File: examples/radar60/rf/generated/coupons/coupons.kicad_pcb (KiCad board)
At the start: 6 copper layers, 60 x 25 mm, 97 parts, among them J60A SMA-J-P-H-ST-EM1, J60B SMA-J-P-H-ST-EM1, J61A SMA-J-P-H-ST-EM1, J61B SMA-J-P-H-ST-EM1, J6RA SMA-J-P-H-ST-EM1, J6RB SMA-J-P-H-ST-EM1

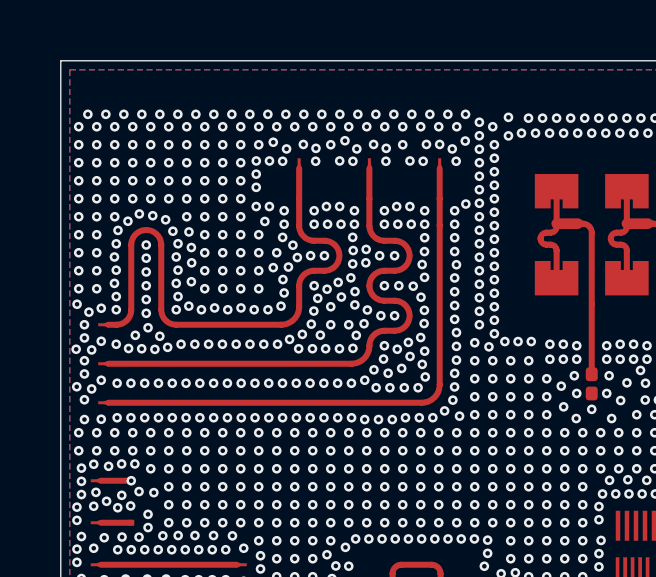
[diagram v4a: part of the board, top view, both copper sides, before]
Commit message: radar60 rf: stage 3b generator options, D14 PA feed, D15 pour variants, E1 models
Generator (examples/radar60/rf/rfmacro):
- D14: the macro owns the VOUT_PA (1V0_PA) feed: A2/B2 bar, a neck east of row A
  inside the package outline, four 0.20/0.40 vias in the pocket (board rules
  unchanged; PWR clearance 0.15 mm), an In3 tie stand-in, board_frame.pa_feed
  hand-off (skip_pads A2/B2). New check G8: clearances, pocket, L2 anti-pads,
  current per via, IR drop [D].
- D15: pour presets A (0.60 mm grid), B (1.00 mm grid, interior hard maximum
  0.75 mm), C (GCPW strips, rings, isolation, load cells; L2-L3 lattice). G3 has
  edge and interior thresholds and an L2-L3 check; stitch metrics per record.
- Dummies S1 / S1.5 and DNP loads ("short" refused); G2 declares the edge
  columns S1 leaves without a neighbour.
- L2-L3 cavity options K0 / K2 (posts, column-congruent) / K1; check G9.
- C1 / D5: div_l_scale and a series-fed column in the bank.
- TX: T2 (R 0.75 north-west finger), T4 (TX1 within a skew budget), T3 order
  planarity; the fit keeps lines out of load mask islands.
- Via placement closes fence gaps a shared row leaves (chain shift, row
  re-plan); known limit: T2's lane-finger junction keeps a 0.65 mm gap (G4).
- `rfmacro variants`: the 14 stage-3b boards; rfm1-m/n/p and coupons rebuilt.

EM (openems): triplet / centre-only cells from the generator, plane-pair
ring-down (board_pp, pp_sim), PA corner (board_pa, pa_sim), mesh templates
(ant_sim --mesh-ref), the E1 campaign builder (stage3b_em.py), results/stage3b.

Co-Authored-By: Claude Opus 5.5 <noreply@anthropic.com>
Claude-Session: https://claude.ai/code/session_014FiHUDEn5jCP4V8pPjQkPy
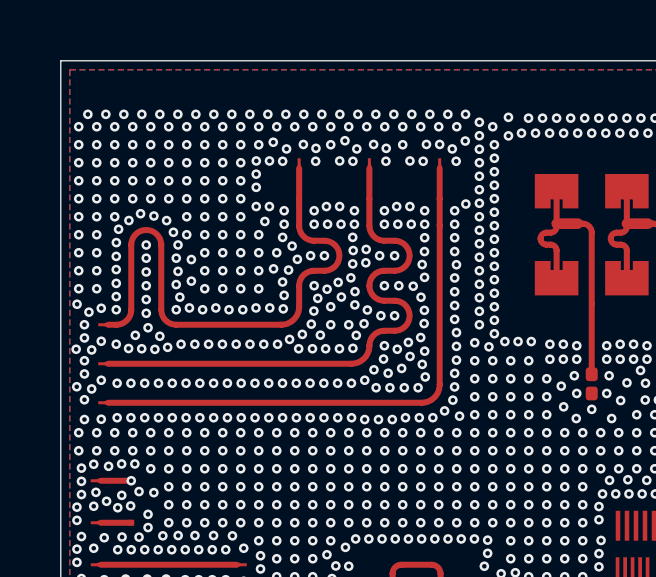
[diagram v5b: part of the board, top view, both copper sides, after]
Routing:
- net GND: vias 1843 -> 1842
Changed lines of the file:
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@@
 	(via (at 113.131 80.9) (size 0.32) (drill 0.15) (layers "F.Cu" "B.Cu") (net "GND"))
 	(via (at 101.85 82.86032) (size 0.32) (drill 0.15) (layers "F.Cu" "B.Cu") (net "GND"))
-	(via (at 101.79 82.42065) (size 0.32) (drill 0.15) (layers "F.Cu" "B.Cu") (net "GND"))
-	(via (at 101.85 81.98097) (size 0.32) (drill 0.15) (layers "F.Cu" "B.Cu") (net "GND"))
-	(via (at 101.79 81.5413) (size 0.32) (drill 0.15) (layers "F.Cu" "B.Cu") (net "GND"))
-	(via (at 101.85079 81.10184) (size 0.32) (drill 0.15) (layers "F.Cu" "B.Cu") (net "GND"))
-	(via (at 101.90842 80.65474) (size 0.32) (drill 0.15) (layers "F.Cu" "B.Cu") (net "GND"))
-	(via (at 102.23992 80.34925) (size 0.32) (drill 0.15) (layers "F.Cu" "B.Cu") (net "GND"))
-	(via (at 102.62 80.10685) (size 0.32) (drill 0.15) (layers "F.Cu" "B.Cu") (net "GND"))
-	(via (at 103.06698 80.16542) (size 0.32) (drill 0.15) (layers "F.Cu" "B.Cu") (net "GND"))
-	(via (at 103.49668 80.30171) (size 0.32) (drill 0.15) (layers "F.Cu" "B.Cu") (net "GND"))
-	(via (at 103.73828 80.6823) (size 0.32) (drill 0.15) (layers "F.Cu" "B.Cu") (net "GND"))
-	(via (at 103.90913 81.09877) (size 0.32) (drill 0.15) (layers "F.Cu" "B.Cu") (net "GND"))
-	(via (at 103.85 81.5413) (size 0.32) (drill 0.15) (layers "F.Cu" "B.Cu") (net "GND"))
-	(via (at 103.91 81.98097) (size 0.32) (drill 0.15) (layers "F.Cu" "B.Cu") (net "GND"))
-	(via (at 103.85 82.42065) (size 0.32) (drill 0.15) (layers "F.Cu" "B.Cu") (net "GND"))
-	(via (at 103.91 82.86032) (size 0.32) (drill 0.15) (layers "F.Cu" "B.Cu") (net "GND"))
-	(via (at 104.26964 83.18) (size 0.32) (drill 0.15) (layers "F.Cu" "B.Cu") (net "GND"))
-	(via (at 104.68928 83.3) (size 0.32) (drill 0.15) (layers "F.Cu" "B.Cu") (net "GND"))
-	(via (at 105.1289 83.24) (size 0.32) (drill 0.15) (layers "F.Cu" "B.Cu") (net "GND"))
-	(via (at 105.56853 83.3) (size 0.32) (drill 0.15) (layers "F.Cu" "B.Cu") (net "GND"))
-	(via (at 106.00815 83.24) (size 0.32) (drill 0.15) (layers "F.Cu" "B.Cu") (net "GND"))
-	(via (at 106.44777 83.3) (size 0.32) (drill 0.15) (layers "F.Cu" "B.Cu") (net "GND"))
-	(via (at 106.90738 83.3) (size 0.32) (drill 0.15) (layers "F.Cu" "B.Cu") (net "GND"))
-	(via (at 107.34246 83.18052) (size 0.32) (drill 0.15) (layers "F.Cu" "B.Cu") (net "GND"))
-	(via (at 107.447 82.74) (size 0.32) (drill 0.15) (layers "F.Cu" "B.Cu") (net "GND"))
-	(via (at 107.40737 82.2932) (size 0.32) (drill 0.15) (layers "F.Cu" "B.Cu") (net "GND"))
-	(via (at 107.58944 81.87695) (size 0.32) (drill 0.15) (layers "F.Cu" "B.Cu") (net "GND"))
-	(via (at 107.88697 81.56) (size 0.32) (drill 0.15) (layers "F.Cu" "B.Cu") (net "GND"))
+	(via (at 101.85 82.42065) (size 0.32) (drill 0.15) (layers "F.Cu" "B.Cu") (net "GND"))
+	(via (at 101.85 81.96099) (size 0.32) (drill 0.15) (layers "F.Cu" "B.Cu") (net "GND"))
+	(via (at 101.85 81.52131) (size 0.32) (drill 0.15) (layers "F.Cu" "B.Cu") (net "GND"))
+	(via (at 101.85316 81.06214) (size 0.32) (drill 0.15) (layers "F.Cu" "B.Cu") (net "GND"))
+	(via (at 101.92852 80.61769) (size 0.32) (drill 0.15) (layers "F.Cu" "B.Cu") (net "GND"))
+	(via (at 102.27191 80.32562) (size 0.32) (drill 0.15) (layers "F.Cu" "B.Cu") (net "GND"))
+	(via (at 102.66132 80.09852) (size 0.32) (drill 0.15) (layers "F.Cu" "B.Cu") (net "GND"))
+	(via (at 103.10562 80.17481) (size 0.32) (drill 0.15) (layers "F.Cu" "B.Cu") (net "GND"))
+	(via (at 103.52956 80.32808) (size 0.32) (drill 0.15) (layers "F.Cu" "B.Cu") (net "GND"))
+	(via (at 103.75584 80.71797) (size 0.32) (drill 0.15) (layers "F.Cu" "B.Cu") (net "GND"))
+	(via (at 103.90998 81.14) (size 0.32) (drill 0.15) (layers "F.Cu" "B.Cu") (net "GND"))
+	(via (at 103.85 81.58127) (size 0.32) (drill 0.15) (layers "F.Cu" "B.Cu") (net "GND"))
+	(via (at 103.91 82.02094) (size 0.32) (drill 0.15) (layers "F.Cu" "B.Cu") (net "GND"))
+	(via (at 103.85 82.46062) (size 0.32) (drill 0.15) (layers "F.Cu" "B.Cu") (net "GND"))
+	(via (at 103.97 82.88031) (size 0.32) (drill 0.15) (layers "F.Cu" "B.Cu") (net "GND"))
+	(via (at 104.28962 83.24) (size 0.32) (drill 0.15) (layers "F.Cu" "B.Cu") (net "GND"))
+	(via (at 104.72925 83.3) (size 0.32) (drill 0.15) (layers "F.Cu" "B.Cu") (net "GND"))
+	(via (at 105.16887 83.24) (size 0.32) (drill 0.15) (layers "F.Cu" "B.Cu") (net "GND"))
+	(via (at 105.60849 83.3) (size 0.32) (drill 0.15) (layers "F.Cu" "B.Cu") (net "GND"))
+	(via (at 106.0681 83.3) (size 0.32) (drill 0.15) (layers "F.Cu" "B.Cu") (net "GND"))
+	(via (at 106.50772 83.24) (size 0.32) (drill 0.15) (layers "F.Cu" "B.Cu") (net "GND"))
+	(via (at 106.96733 83.24) (size 0.32) (drill 0.15) (layers "F.Cu" "B.Cu") (net "GND"))
+	(via (at 107.41771 83.27071) (size 0.32) (drill 0.15) (layers "F.Cu" "B.Cu") (net "GND"))
+	(via (at 107.447 82.82) (size 0.32) (drill 0.15) (layers "F.Cu" "B.Cu") (net "GND"))
+	(via (at 107.39435 82.37541) (size 0.32) (drill 0.15) (layers "F.Cu" "B.Cu") (net "GND"))
+	(via (at 107.59436 81.9775) (size 0.32) (drill 0.15) (layers "F.Cu" "B.Cu") (net "GND"))
+	(via (at 107.88697 81.62) (size 0.32) (drill 0.15) (layers "F.Cu" "B.Cu") (net "GND"))
 	(via (at 108.32864 81.5) (size 0.32) (drill 0.15) (layers "F.Cu" "B.Cu") (net "GND"))
+	(via (at 107.71268 81.1788) (size 0.32) (drill 0.15) (layers "F.Cu" "B.Cu") (net "GND"))
 	(via (at 107.39623 80.88765) (size 0.32) (drill 0.15) (layers "F.Cu" "B.Cu") (net "GND"))
 	(via (at 101.85 84.45) (size 0.32) (drill 0.15) (layers "F.Cu" "B.Cu") (net "GND"))
@@
 	(via (at 113.191 81.8) (size 0.32) (drill 0.15) (layers "F.Cu" "B.Cu") (net "GND"))
 	(via (at 113.131 81.36) (size 0.32) (drill 0.15) (layers "F.Cu" "B.Cu") (net "GND"))
-	(via (at 107.73921 81.14902) (size 0.32) (drill 0.15) (layers "F.Cu" "B.Cu") (net "GND"))
 	(via (at 102.69864 84.6) (size 0.32) (drill 0.15) (layers "F.Cu" "B.Cu") (net "GND"))
 	(via (at 107.93139 84.6) (size 0.32) (drill 0.15) (layers "F.Cu" "B.Cu") (net "GND"))
@@
 	(via (at 104.2 88) (size 0.32) (drill 0.15) (layers "F.Cu" "B.Cu") (net "GND"))
 	(via (at 104.2 87.4) (size 0.32) (drill 0.15) (layers "F.Cu" "B.Cu") (net "GND"))
+	(via (at 104.2 80.8) (size 0.32) (drill 0.15) (layers "F.Cu" "B.Cu") (net "GND"))
 	(via (at 104.2 80.2) (size 0.32) (drill 0.15) (layers "F.Cu" "B.Cu") (net "GND"))
 	(via (at 104.2 79.6) (size 0.32) (drill 0.15) (layers "F.Cu" "B.Cu") (net "GND"))
@@
 	(via (at 109.91371 97.78629) (size 0.32) (drill 0.15) (layers "F.Cu" "B.Cu") (net "GND"))
 	(via (at 122.10371 91.59629) (size 0.32) (drill 0.15) (layers "F.Cu" "B.Cu") (net "GND"))
-	(via (at 104.35371 81.22629) (size 0.32) (drill 0.15) (layers "F.Cu" "B.Cu") (net "GND"))
 	(via (at 126.62371 76.81629) (size 0.32) (drill 0.15) (layers "F.Cu" "B.Cu") (net "GND"))
 	(via (at 104.13371 94.07629) (size 0.32) (drill 0.15) (layers "F.Cu" "B.Cu") (net "GND"))
@@
 	(via (at 105.72371 90.83629) (size 0.32) (drill 0.15) (layers "F.Cu" "B.Cu") (net "GND"))
 	(via (at 126.21371 85.88629) (size 0.32) (drill 0.15) (layers "F.Cu" "B.Cu") (net "GND"))
+	(via (at 104.35371 81.62629) (size 0.32) (drill 0.15) (layers "F.Cu" "B.Cu") (net "GND"))
 	(via (at 122.88371 86.91629) (size 0.32) (drill 0.15) (layers "F.Cu" "B.Cu") (net "GND"))
 	(via (at 100.53371 85.86629) (size 0.32) (drill 0.15) (layers "F.Cu" "B.Cu") (net "GND"))
@@
 	(via (at 126.10371 76.78629) (size 0.32) (drill 0.15) (layers "F.Cu" "B.Cu") (net "GND"))
 	(via (at 115.67371 97.71629) (size 0.32) (drill 0.15) (layers "F.Cu" "B.Cu") (net "GND"))
-	(via (at 104.35371 82.36629) (size 0.32) (drill 0.15) (layers "F.Cu" "B.Cu") (net "GND"))
+	(via (at 104.35371 82.34629) (size 0.32) (drill 0.15) (layers "F.Cu" "B.Cu") (net "GND"))
 	(via (at 107.05371 94.99629) (size 0.32) (drill 0.15) (layers "F.Cu" "B.Cu") (net "GND"))
 	(via (at 107.03371 96.70629) (size 0.32) (drill 0.15) (layers "F.Cu" "B.Cu") (net "GND"))
@@
 	(via (at 135.22371 90.47629) (size 0.32) (drill 0.15) (layers "F.Cu" "B.Cu") (net "GND"))
 	(via (at 108.49371 97.76629) (size 0.32) (drill 0.15) (layers "F.Cu" "B.Cu") (net "GND"))
-	(via (at 107.08371 81.89629) (size 0.32) (drill 0.15) (layers "F.Cu" "B.Cu") (net "GND"))
+	(via (at 107.09371 81.93629) (size 0.32) (drill 0.15) (layers "F.Cu" "B.Cu") (net "GND"))
 	(via (at 101.17371 89.38629) (size 0.32) (drill 0.15) (layers "F.Cu" "B.Cu") (net "GND"))
 	(via (at 108.70371 76.78629) (size 0.32) (drill 0.15) (layers "F.Cu" "B.Cu") (net "GND"))
@@
 	(via (at 134.50371 77.52629) (size 0.32) (drill 0.15) (layers "F.Cu" "B.Cu") (net "GND"))
 	(via (at 134.49371 98.73629) (size 0.32) (drill 0.15) (layers "F.Cu" "B.Cu") (net "GND"))
-	(via (at 104.36371 81.73629) (size 0.32) (drill 0.15) (layers "F.Cu" "B.Cu") (net "GND"))
 	(via (at 128.42371 79.78629) (size 0.32) (drill 0.15) (layers "F.Cu" "B.Cu") (net "GND"))
 	(via (at 125.85371 90.26629) (size 0.32) (drill 0.15) (layers "F.Cu" "B.Cu") (net "GND"))
@@
 	(via (at 103.51371 92.27629) (size 0.32) (drill 0.15) (layers "F.Cu" "B.Cu") (net "GND"))
 	(via (at 124.70371 78.61629) (size 0.32) (drill 0.15) (layers "F.Cu" "B.Cu") (net "GND"))
-	(via (at 104.27371 80.70629) (size 0.32) (drill 0.15) (layers "F.Cu" "B.Cu") (net "GND"))
 	(via (at 111.64371 84.85629) (size 0.32) (drill 0.15) (layers "F.Cu" "B.Cu") (net "GND"))
 	(via (at 120.51371 94.62629) (size 0.32) (drill 0.15) (layers "F.Cu" "B.Cu") (net "GND"))

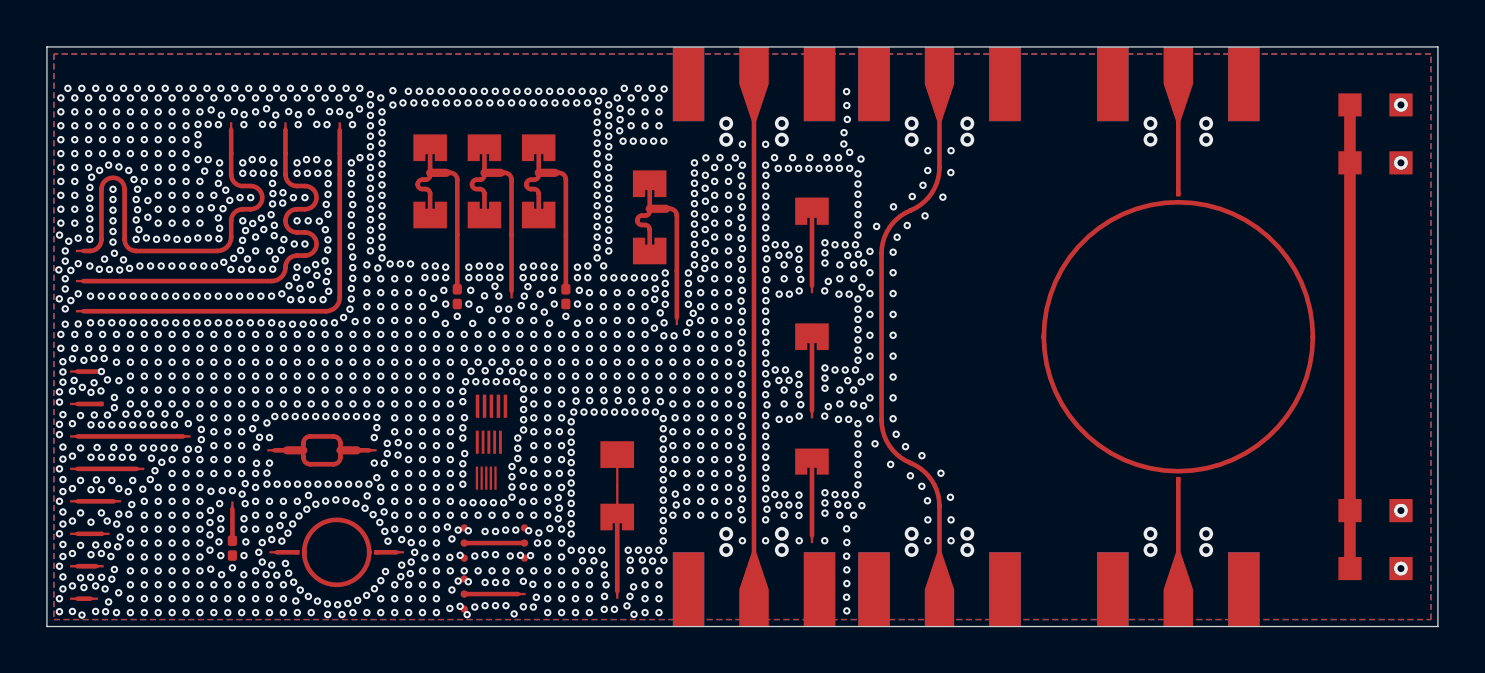
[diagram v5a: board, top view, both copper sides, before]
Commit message: radar60 rf: freeze macro v2 (stage 3b): C1 column pick, rfm1-m/n/p, coupons, board_frame
- rfmacro params: the C1 rule's pick (embedded centre column, cell-c1b-6, K0, 20 um):
  fullwave_l_scale 1.025, inset 0.325, w35 0.42, t_y 0.25. Worst in-band |S11| -6.5 dB
  (-7.2 dB Palace-referred); ANT-02 RL miss preregistered. K1 at L 1.00/1.015/1.03
  (s3b-e3) never reaches -10 dB (best -8.8 dB), so K0 stays per the K rule.
- regenerated rfm1-m/-n/-p and coupons with the frozen defaults (S1 outer dummies, D14 PA
  feed + fence, D15 A, C1); KiCad DRC 0 violations, 0 unconnected on all three.
- board/floorplan.yaml follows the new board_frame: height 47.40 (min 47.384), patches,
  region, pocket (now 1.69 x 1.55), guard, mounting holes; gen_board --macro all covered.
- tests: expectations updated for the S1 default (were failing at HEAD since the S1/fence
  freeze); series/T4 option tests pin S2 dummies (under S1 they leave a G4 fence gap).

Co-Authored-By: Claude Opus 5.5 <noreply@anthropic.com>
Claude-Session: https://claude.ai/code/session_01XmUgXgxLjzBpn2W6JpqE2p
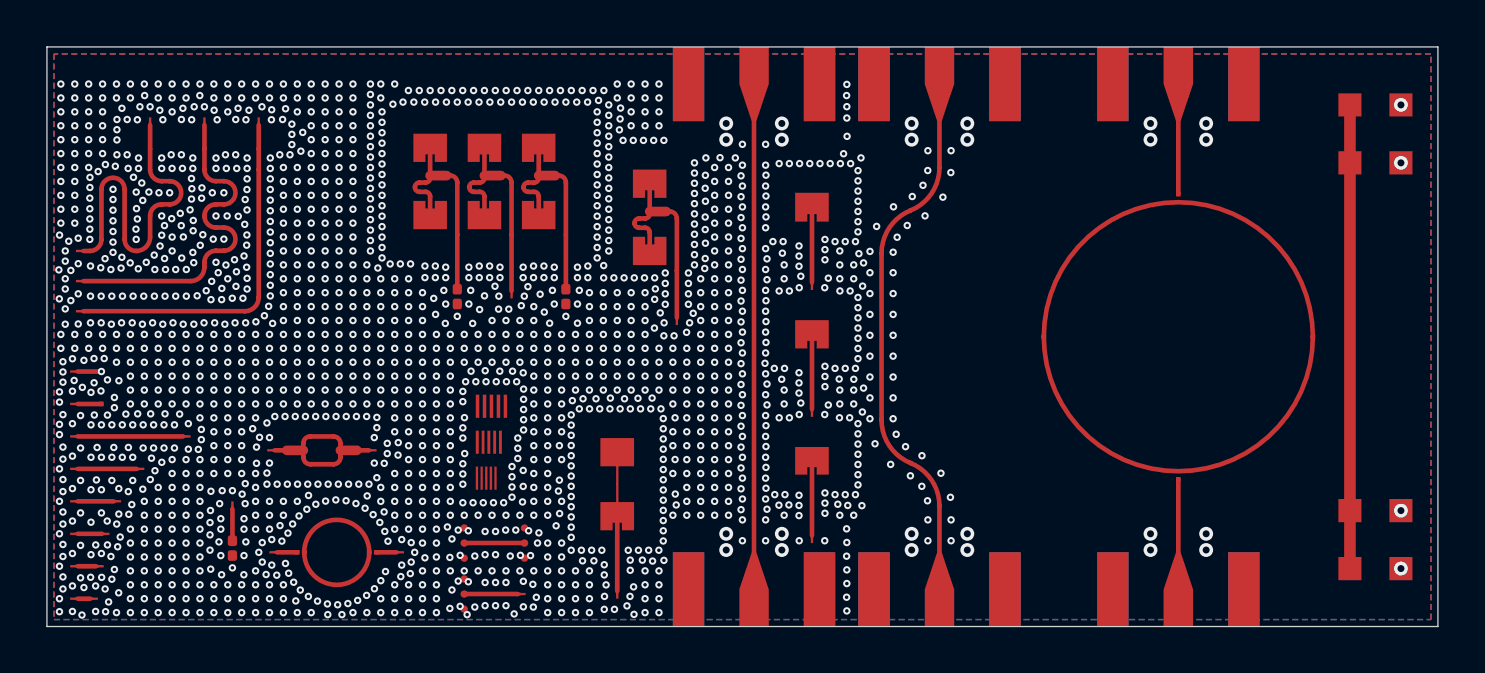
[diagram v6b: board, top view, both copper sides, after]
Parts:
- moved CP54 3.50 mm to (104.5, 78.2)
- moved CP56 3.50 mm to (106.8, 78.2)
- moved CP58 3.50 mm to (109.1, 78.2)
- moved CP73 0.17 mm to (133.0, 81.9)
- moved CP74 0.14 mm to (133.0, 85.3)
- moved CP50 0.10 mm to (124.6, 92.5)
- moved CP71 0.10 mm to (133.0, 87.4)
- moved CP51 0.07 mm to (124.6, 93.9)
- moved CP72 0.07 mm to (133.0, 90.8)
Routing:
- net CPT_TX3: track 18.5 -> 15.3 mm
- net CPT_TX1: track 18.2 -> 14.9 mm
- net CPT_TX2: track 18.2 -> 14.9 mm
- net GND: vias 1842 -> 1851
